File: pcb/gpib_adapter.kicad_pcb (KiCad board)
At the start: 2 copper layers, 23 parts, among them P1 TC2030-MCP, P2 USB, P5 GPIB, U1 SN75160, U2 SN75161, U3 PIC18(L)F4550-I/PT, X1 8MHz

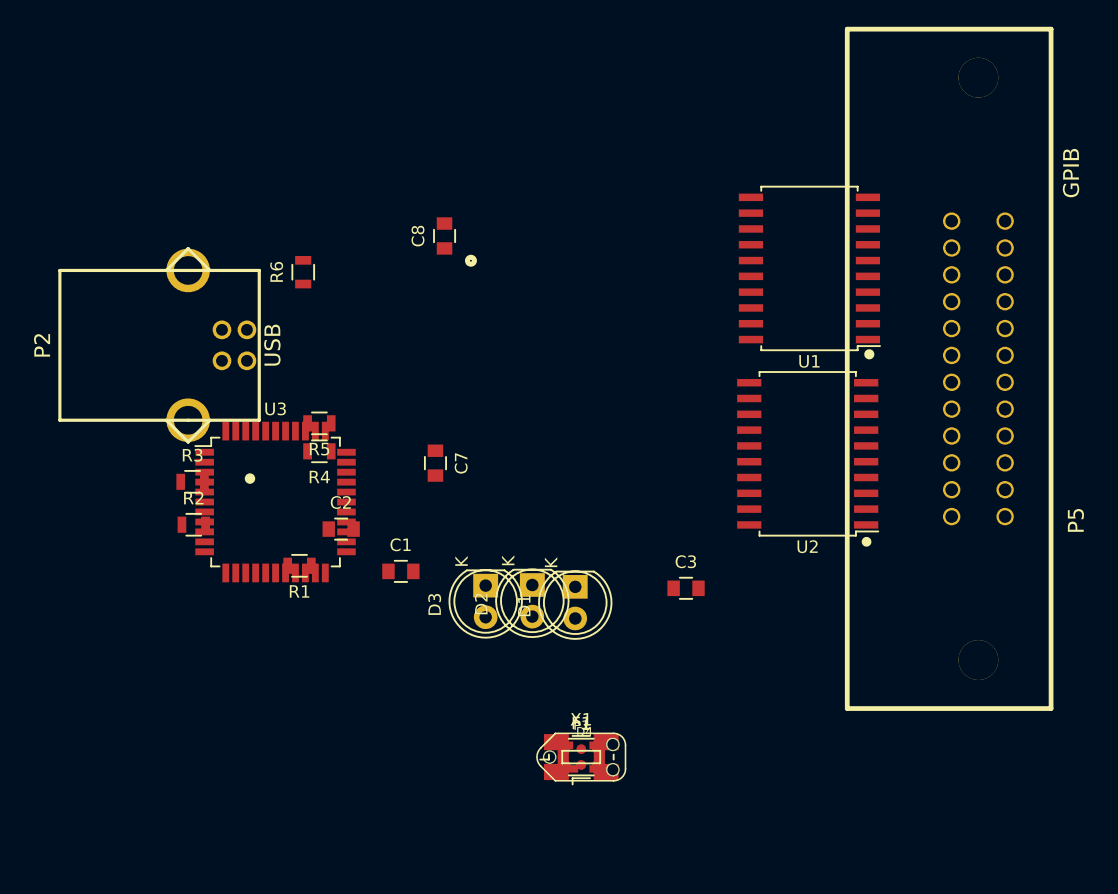
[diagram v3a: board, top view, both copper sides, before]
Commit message: Update pcb files. New version based on pic 18f4550.
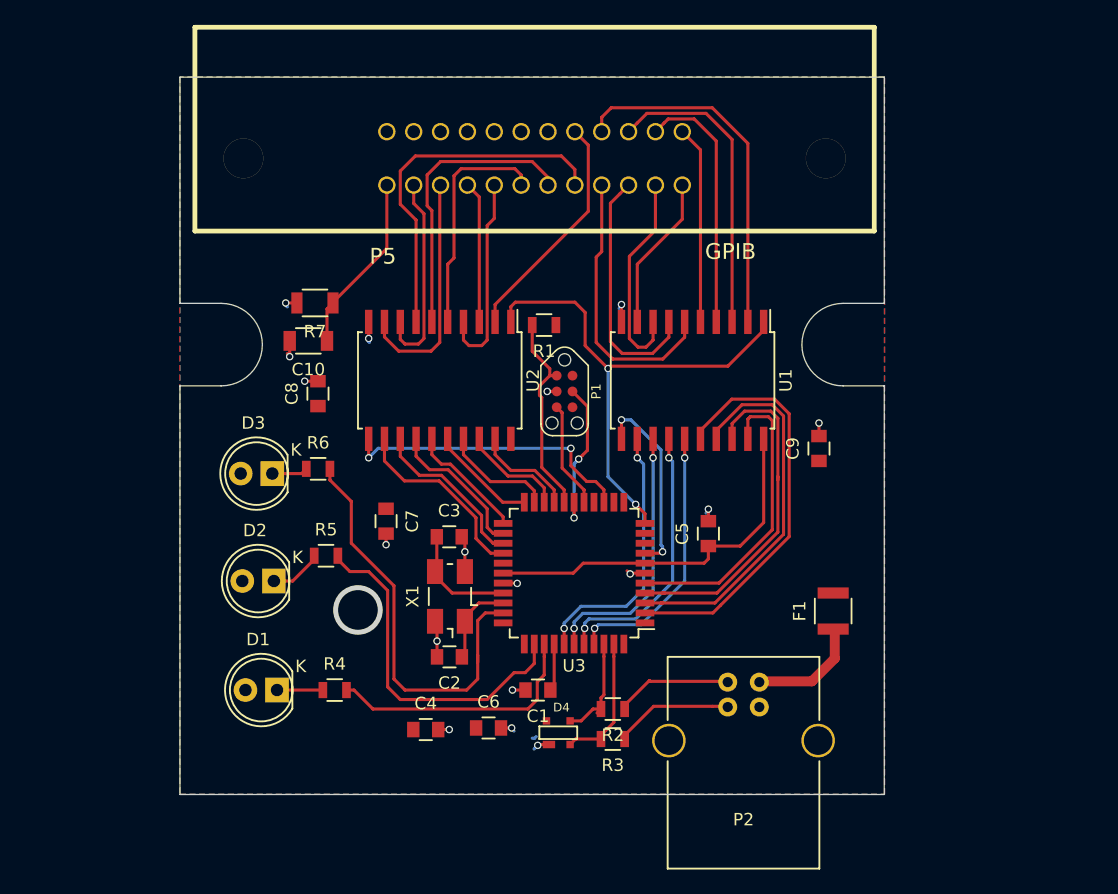
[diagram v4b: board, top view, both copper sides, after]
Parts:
- added C10: C, Capacitors_SMD:C_1206, F.Cu at (126.0, 91.8)
- added C4: 100n, Capacitors_SMD:C_0805, F.Cu at (135.4, 123.1)
- added C5: 100n, Capacitors_SMD:C_0805, F.Cu at (158.1, 107.3)
- added C6: 10n, Capacitors_SMD:C_0805, F.Cu at (140.4, 122.9)
- added C9: 10n, Capacitors_SMD:C_0805, F.Cu at (167.0, 100.5)
- added R7: R, Resistors_SMD:R_1206, F.Cu at (126.5, 88.8)
- P2: footprint w_conn_pc:conn_usb_B -> Connect:USB_B
- moved P2 55.3 mm to (162.2, 119.3)
- moved R3 39.6 mm to (150.4, 123.8), turned to 180 degrees
- moved P5 39.5 mm to (144.1, 77.2), turned to 180 degrees
- moved R2 36.8 mm to (150.4, 121.4), turned to 180 degrees
- moved U2 30.2 mm to (136.5, 95.0), turned to 270 degrees
- moved P1 29.4 mm to (146.6, 95.9), turned to 270 degrees
- moved R1 27.6 mm to (144.9, 90.6)
- moved D1 25.4 mm to (123.4, 119.9), turned to 180 degrees
- moved U3 24.7 mm to (147.3, 110.5), turned to 180 degrees
- moved F1 23.4 mm to (168.1, 113.5), turned to 90 degrees
- moved D2 20.8 mm to (123.2, 111.1), turned to 180 degrees
- moved C3 19.5 mm to (137.3, 107.6)
- moved D3 19.4 mm to (123.1, 102.5), turned to 180 degrees
- moved R4 19.2 mm to (128.1, 119.9), turned to 0 degrees
- moved X1 16.7 mm to (137.3, 112.4), turned to 90 degrees
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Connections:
- net /RXD renamed Net-(U3-Pad9)
- net /TXD renamed Net-(U3-Pad10)
- P5 pad 10: /REN B -> /SRQ B
- P5 pad 11: /DAV B -> /ATN B
- P5 pad 12: GND -> Net-(C10-Pad1)
- P5 pad 13: /NRFD B -> /DIO5 B
- P5 pad 14: GND -> /DIO6 B
- P5 pad 15: /NDAC B -> /DIO7 B
- P5 pad 16: GND -> /DIO8 B
- P5 pad 17: /IFC B -> /REN B
- P5 pad 19: /SRQ B -> GND
- P5 pad 2: /DIO5 B -> /DIO2 B
- P5 pad 21: /ATN B -> GND
- P5 pad 3: /DIO2 B -> /DIO3 B
- P5 pad 4: /DIO6 B -> /DIO4 B
- P5 pad 5: /DIO3 B -> /EOI B
- P5 pad 6: /DIO7 B -> /DAV B
- P5 pad 7: /DIO4 B -> /NRFD B
- P5 pad 8: /DIO8 B -> /NDAC B
- P5 pad 9: /EOI B -> /IFC B
- U3 pad 1: /ATN -> Net-(U3-Pad1)
- U3 pad 25: /GPIO1 -> /ATN
- U3 pad 26: /SCK -> /SRQ
- U3 pad 27: /ATN -> Net-(U3-Pad27)
- U3 pad 44: /SRQ -> Net-(U3-Pad44)
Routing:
- net /TE: track 0.00 -> 41.1 mm, vias 0 -> 2
- net /PWR: track 0.00 -> 34.1 mm
- net /DIO5: track 0.00 -> 33.3 mm
- net /DIO6: track 0.00 -> 30.4 mm
- net +5V: track 0.00 -> 30.0 mm
- net /EOI B: track 0.00 -> 28.9 mm
- net /DIO8 B: track 0.00 -> 28.8 mm
- net /MODE: track 0.00 -> 28.1 mm
- net /DIO7: track 0.00 -> 27.9 mm
- net GND: track 0.00 -> 24.6 mm, vias 0 -> 17
- net /DIO8: track 0.00 -> 24.5 mm
- net /DIO7 B: track 0.00 -> 24.5 mm
- net /DC: track 0.00 -> 23.9 mm, vias 0 -> 2
- net /DAV B: track 0.00 -> 23.3 mm
- net /DIO4 B: track 0.00 -> 23.1 mm
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- added copper zone on F.Cu, net +5V
- added copper zone on B.Cu, net GND
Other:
- board outline added: 56.6 x 57.7 mm
- board text added: "14.31 [.563]"
- board text added: "14.83 [.584]"
- board text added: "18.18 [.716]"
- board text added: "24/06/2016"
- board text added: "28.00 [1.102]"
- board text added: "56.61 [2.229]"
- board text added: "57.66 [2.270]"
- board text added: "6.62 [.261]"
- board text added: "6.63 [.261]"
- board text added: "GPIB2USB V2.0"
- board text added: "https://github.com/asanza/gpib2usb"
- board text added: "∅3.20 { x 4}\X[.126]"

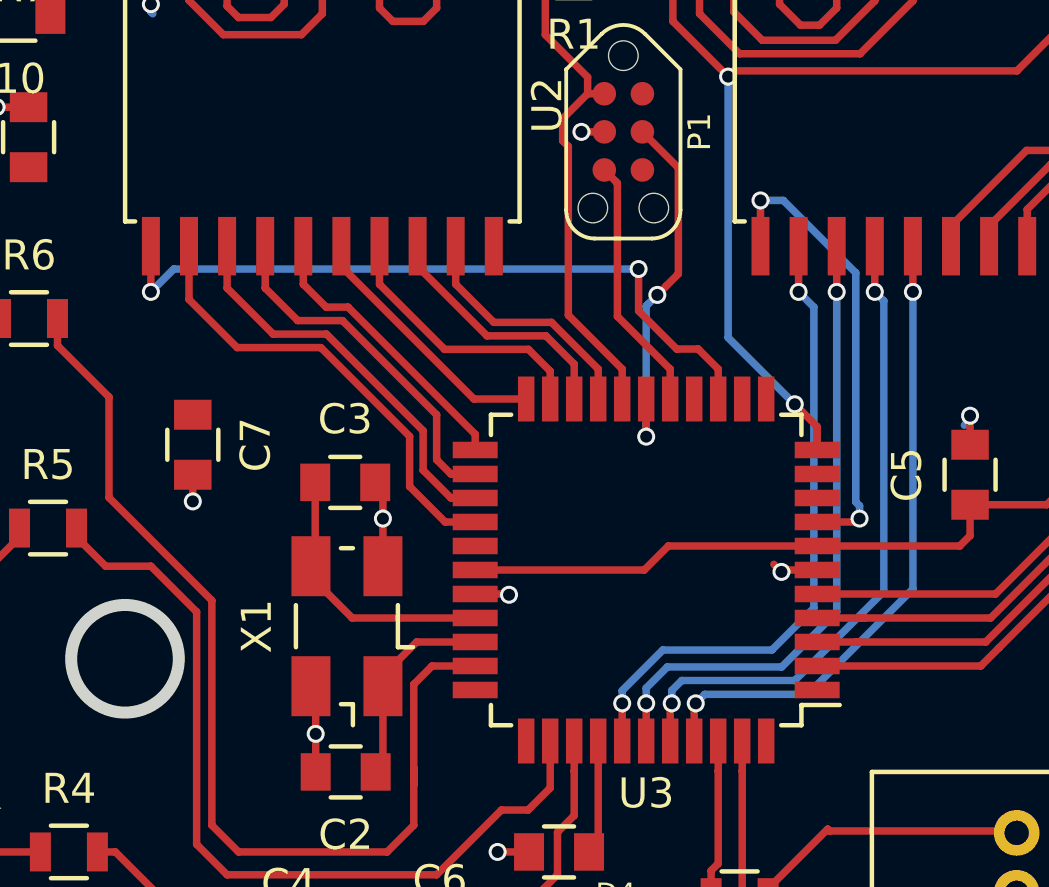
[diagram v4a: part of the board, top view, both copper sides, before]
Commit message: change srq to pin rb0 to make it use the external interrupt 0
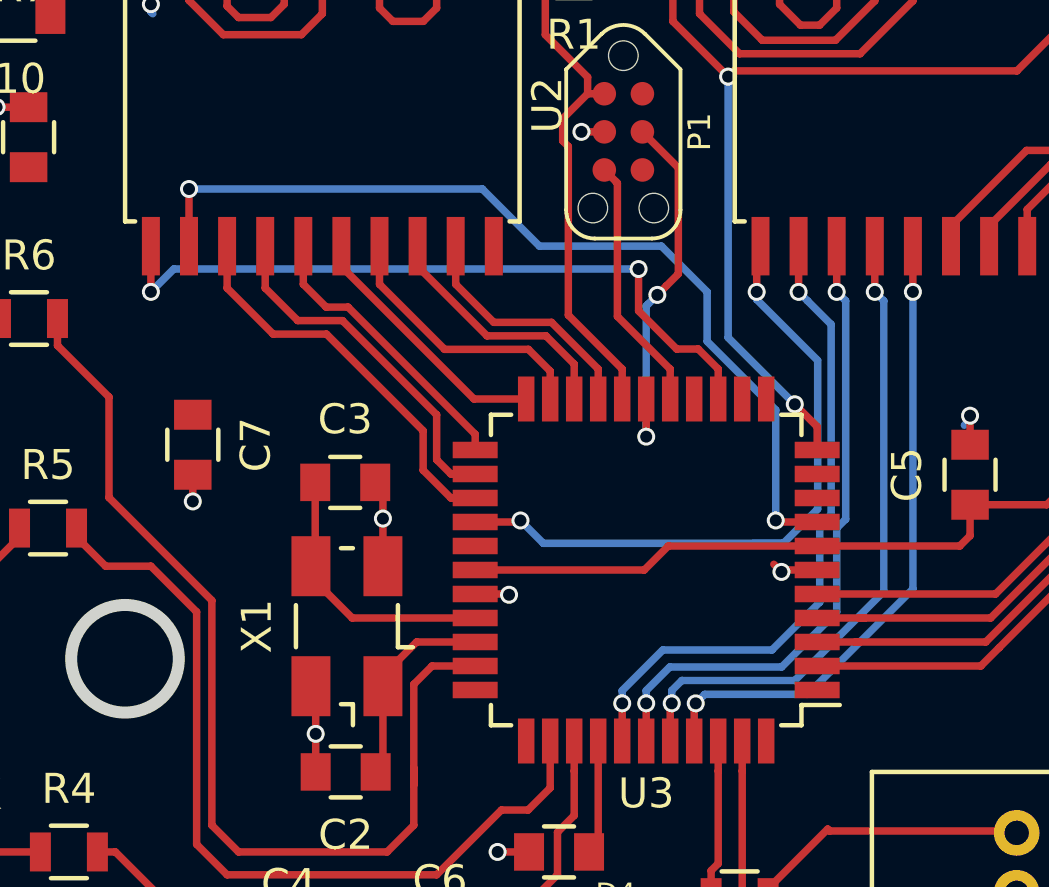
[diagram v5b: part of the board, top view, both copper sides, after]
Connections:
- U3 pad 26: /SRQ -> /PE
- U3 pad 8: /PE -> /SRQ
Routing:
- net /SRQ: track 15.4 -> 30.7 mm, vias 0 -> 2
- net /PE: track 15.4 -> 22.9 mm
